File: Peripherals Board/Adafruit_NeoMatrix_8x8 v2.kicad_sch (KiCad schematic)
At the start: 8 parts, among them J1 Conn_01x03_Pin, J2 Conn_01x02_Pin, J3 Conn_01x10_Pin, J4 Conn_01x10_Pin, J5 Conn_01x02_Pin, U1 Teensy4.0, U2 74AHC125, U3 SN65HVD230

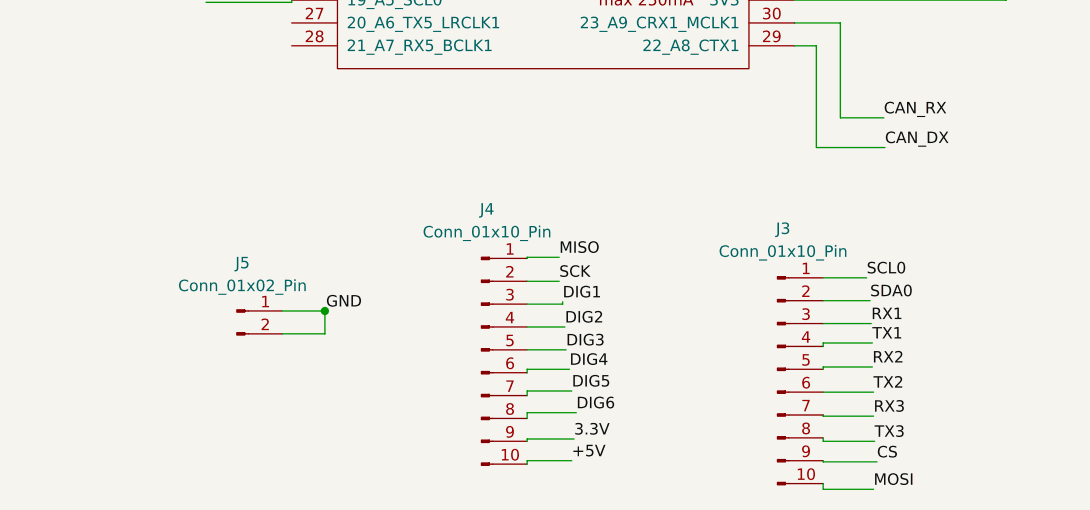
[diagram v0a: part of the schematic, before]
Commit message: Add footprints and layouts
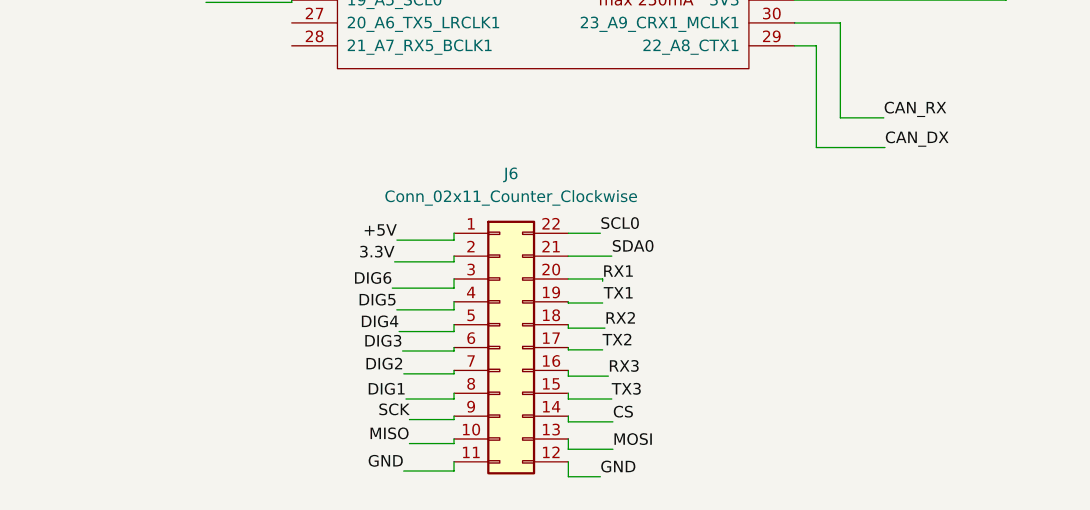
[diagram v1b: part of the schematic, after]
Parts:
- removed J3, J4: Conn_01x10_Pin, symbol Connector:Conn_01x10_Pin
- removed J5: Conn_01x02_Pin, symbol Connector:Conn_01x02_Pin
- added J6: Conn_02x11_Counter_Clockwise, Connector_PinSocket_2.54mm:PinSocket_2x11_P2.54mm_Vertical, symbol Connector_Generic:Conn_02x11_Counter_Clockwise
- J1: footprint (none) -> Connector_JST:JST_GH_SM03B-GHS-TB_1x03-1MP_P1.25mm_Horizontal
- J2: footprint (none) -> Connector_JST:JST_GH_SM02B-GHS-TB_1x02-1MP_P1.25mm_Horizontal
- U1: footprint (none) -> teensy:Teensy40
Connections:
- net +5V: now also J6.1 (Pin_1)
- net 3.3V: now also J6.2 (Pin_2)
- net CS: now also J6.14 (Pin_14)
- net DIG1: now also J6.8 (Pin_8)
- net DIG2: now also J6.7 (Pin_7)
- net DIG3: now also J6.6 (Pin_6)
- net DIG4: now also J6.5 (Pin_5)
- net DIG5: now also J6.4 (Pin_4)
- net DIG6: now also J6.3 (Pin_3)
- net GND: now also J6.11 (Pin_11), J6.12 (Pin_12)
- net MISO: now also J6.10 (Pin_10)
- net MOSI: now also J6.13 (Pin_13)
- net RX1: now also J6.20 (Pin_20)
- net RX2: now also J6.18 (Pin_18)
- net RX3: now also J6.16 (Pin_16)
- net SCK: now also J6.9 (Pin_9)
- net SCL0: now also J6.22 (Pin_22)
- net SDA0: now also J6.21 (Pin_21)
- net TX2: now also J6.17 (Pin_17)
- net TX3: now also J6.15 (Pin_15)
